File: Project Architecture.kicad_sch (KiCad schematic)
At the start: 0 parts

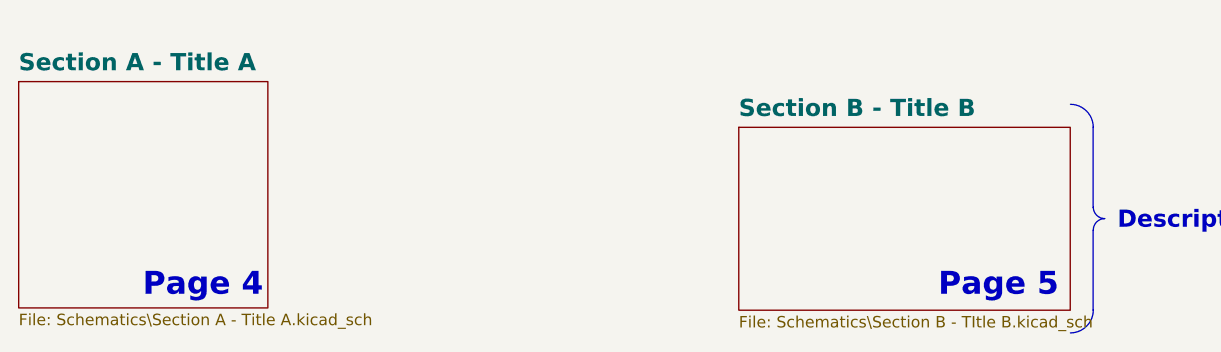
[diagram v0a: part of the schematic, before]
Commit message: Add Power Budget Sheet
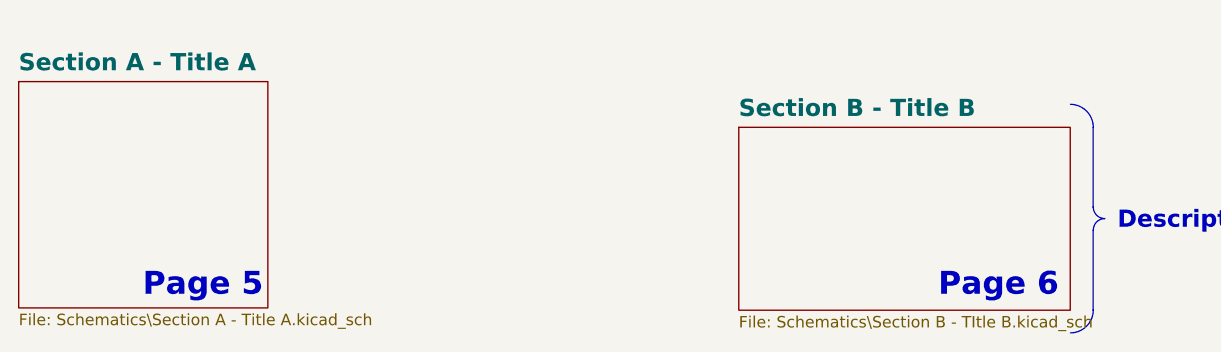
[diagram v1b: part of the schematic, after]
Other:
- note added: "Page 6"
- note removed: "Page 4"
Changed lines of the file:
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@@
 		)
 	)
-	(text "Page 4"
+	(text "Page 5"
 		(exclude_from_sim no)
 		(at 151.638 104.14 0)
@@
 			)
 			(justify right bottom)
-			(href "#4")
+			(href "#5")
 		)
 	)
-	(text "Page 5"
+	(text "Page 6"
 		(exclude_from_sim no)
 		(at 240.03 104.14 0)
@@
 			)
 			(justify right bottom)
-			(href "#5")
+			(href "#6")
 		)
 	)
@@
 			(project "SkyForge_Controller"
 				(path "/0650c7a8-acba-429c-9f8e-eec0baf0bc1c/fede4c36-00cc-4d3d-b71c-5243ba232202"
-					(page "4")
+					(page "5")
 				)
 			)
@@
 			(project "SkyForge_Controller"
 				(path "/0650c7a8-acba-429c-9f8e-eec0baf0bc1c/fede4c36-00cc-4d3d-b71c-5243ba232202"
-					(page "5")
+					(page "6")
 				)
 			)

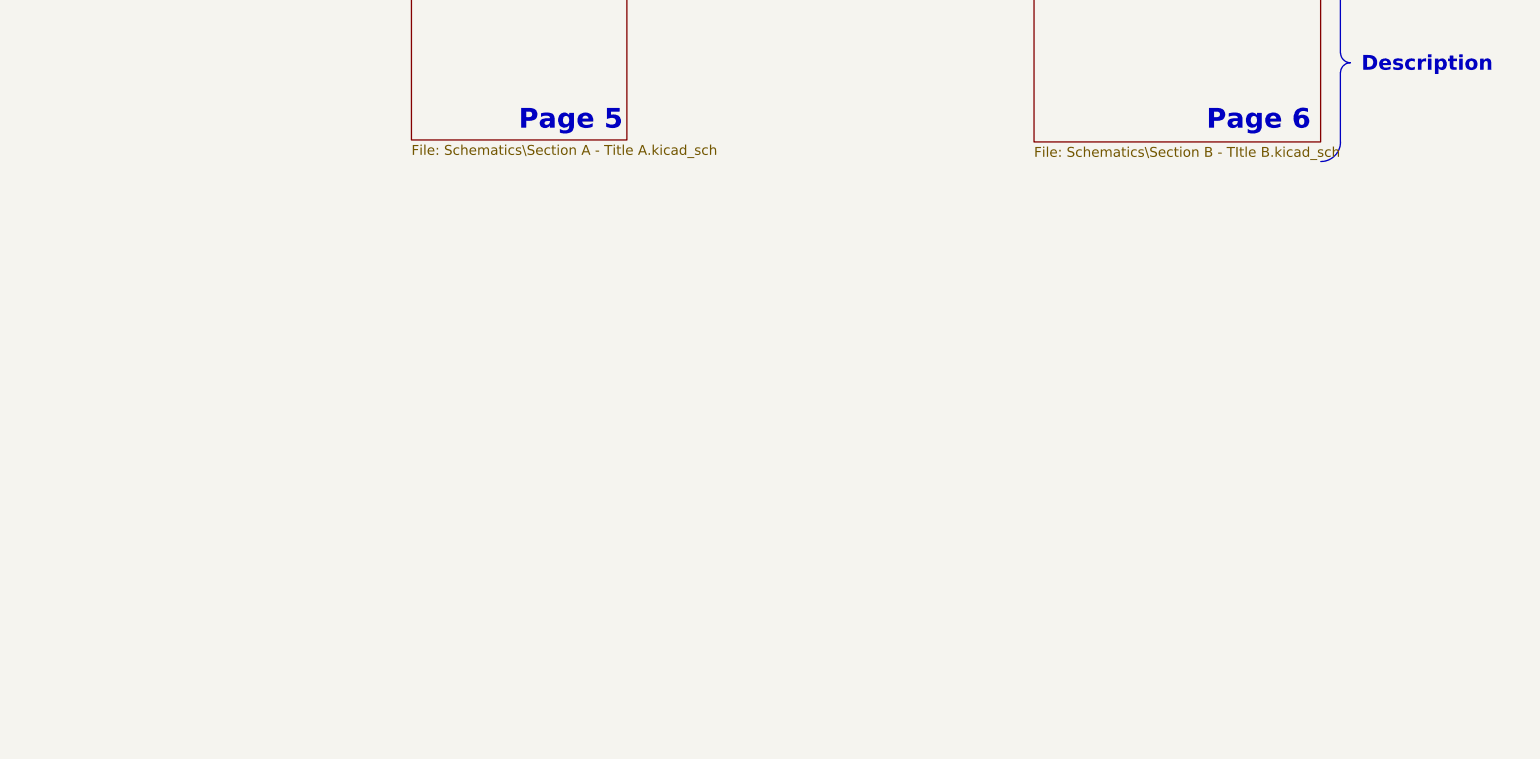
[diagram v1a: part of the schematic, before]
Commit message: Add MCU to schematic
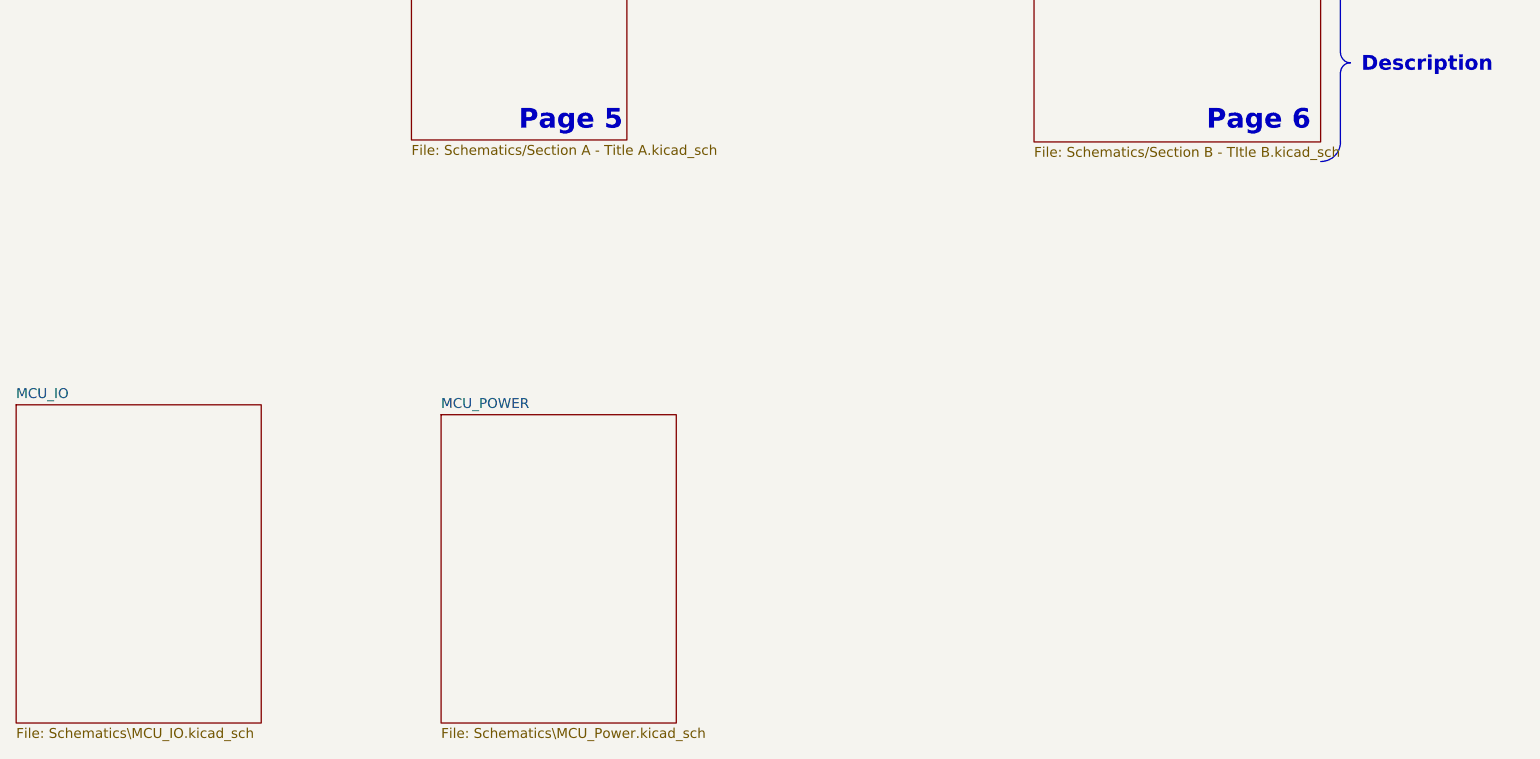
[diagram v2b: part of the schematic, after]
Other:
- added sheet MCU_IO (Schematics\MCU_IO.kicad_sch)
- added sheet MCU_POWER (Schematics\MCU_Power.kicad_sch)
- sheet Section A - Title A: file Schematics\Section A - Title A.kicad_sch -> Schematics/Section A - Title A.kicad_sch
- sheet Section B - Title B: file Schematics\Section B - TItle B.kicad_sch -> Schematics/Section B - TItle B.kicad_sch
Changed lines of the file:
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@@
+	)
+	(sheet
+		(at 73.66 139.192)
+		(size 31.496 40.894)
+		(exclude_from_sim no)
+		(in_bom yes)
+		(on_board yes)
+		(dnp no)
+		(fields_autoplaced yes)
+		(stroke
+			(width 0.1524)
+			(type solid)
+		)
+		(fill
+			(color 0 0 0 0)
+		)
+		(property "Sheetname" "MCU_IO"
+			(at 73.66 138.4804 0)
+			(show_name no)
+			(do_not_autoplace no)
+			(effects
+				(font
+					(size 1.27 1.27)
+				)
+				(justify left bottom)
+			)
+		)
+		(property "Sheetfile" "Schematics\\MCU_IO.kicad_sch"
+			(at 73.66 180.6706 0)
+			(show_name no)
+			(do_not_autoplace no)
+			(effects
+				(font
+					(size 1.27 1.27)
+				)
+				(justify left top)
+			)
+		)
+		(instances
+			(project "SkyForge_Controller"
+				(path "/0650c7a8-acba-429c-9f8e-eec0baf0bc1c/fede4c36-00cc-4d3d-b71c-5243ba232202"
+					(page "8")
+				)
+			)
+		)
 	)
 	(sheet
@@
 			)
 		)
-		(property "Sheetfile" "Schematics\\Section A - Title A.kicad_sch"
+		(property "Sheetfile" "Schematics/Section A - Title A.kicad_sch"
 			(at 124.46 105.7406 0)
 			(show_name no)
@@
 				(path "/0650c7a8-acba-429c-9f8e-eec0baf0bc1c/fede4c36-00cc-4d3d-b71c-5243ba232202"
 					(page "5")
+				)
+			)
+		)
+	)
+	(sheet
+		(at 128.27 140.462)
+		(size 30.226 39.624)
+		(exclude_from_sim no)
+		(in_bom yes)
+		(on_board yes)
+		(dnp no)
+		(fields_autoplaced yes)
+		(stroke
+			(width 0.1524)
+			(type solid)
+		)
+		(fill
+			(color 0 0 0 0)
+		)
+		(property "Sheetname" "MCU_POWER"
+			(at 128.27 139.7504 0)
+			(show_name no)
+			(do_not_autoplace no)
+			(effects
+				(font
+					(size 1.27 1.27)
+				)
+				(justify left bottom)
+			)
+		)
+		(property "Sheetfile" "Schematics\\MCU_Power.kicad_sch"
+			(at 128.27 180.6706 0)
+			(show_name no)
+			(do_not_autoplace no)
+			(effects
+				(font
+					(size 1.27 1.27)
+				)
+				(justify left top)
+			)
+		)
+		(instances
+			(project "SkyForge_Controller"
+				(path "/0650c7a8-acba-429c-9f8e-eec0baf0bc1c/fede4c36-00cc-4d3d-b71c-5243ba232202"
+					(page "9")
 				)
 			)
@@
 			)
 		)
-		(property "Sheetfile" "Schematics\\Section B - TItle B.kicad_sch"
+		(property "Sheetfile" "Schematics/Section B - TItle B.kicad_sch"
 			(at 204.47 105.9946 0)
 			(show_name no)

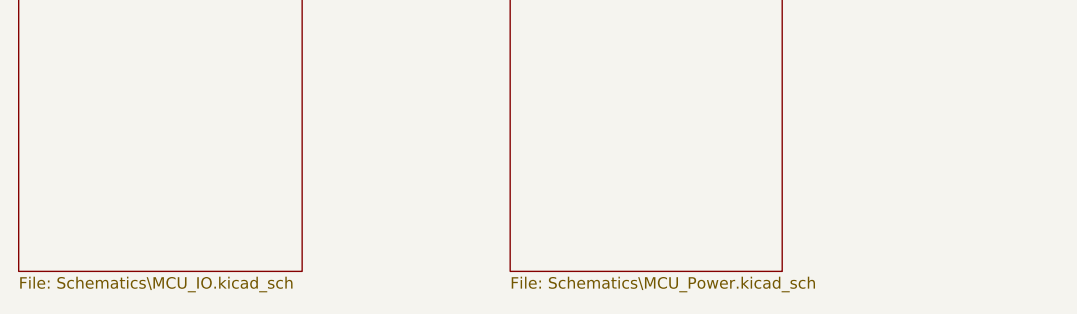
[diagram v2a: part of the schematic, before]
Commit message: Add MCU Power schematic
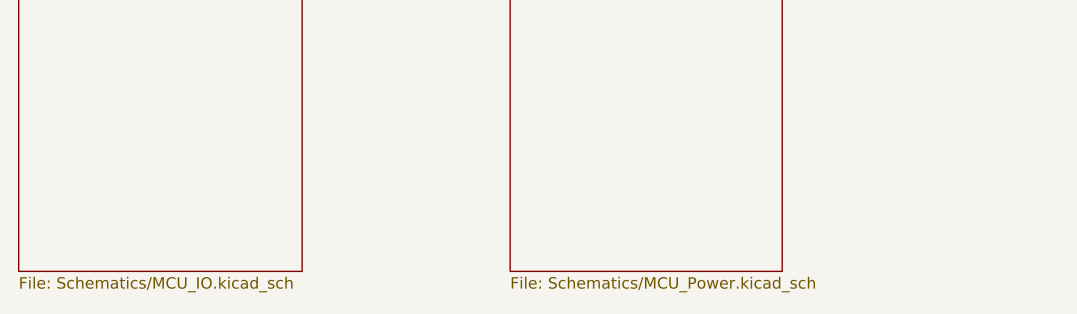
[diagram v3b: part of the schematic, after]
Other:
- sheet MCU_IO: file Schematics\MCU_IO.kicad_sch -> Schematics/MCU_IO.kicad_sch
- sheet MCU_POWER: file Schematics\MCU_Power.kicad_sch -> Schematics/MCU_Power.kicad_sch
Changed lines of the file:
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@@
 			)
 		)
-		(property "Sheetfile" "Schematics\\MCU_IO.kicad_sch"
+		(property "Sheetfile" "Schematics/MCU_IO.kicad_sch"
 			(at 73.66 180.6706 0)
 			(show_name no)
@@
 			)
 		)
-		(property "Sheetfile" "Schematics\\MCU_Power.kicad_sch"
+		(property "Sheetfile" "Schematics/MCU_Power.kicad_sch"
 			(at 128.27 180.6706 0)
 			(show_name no)

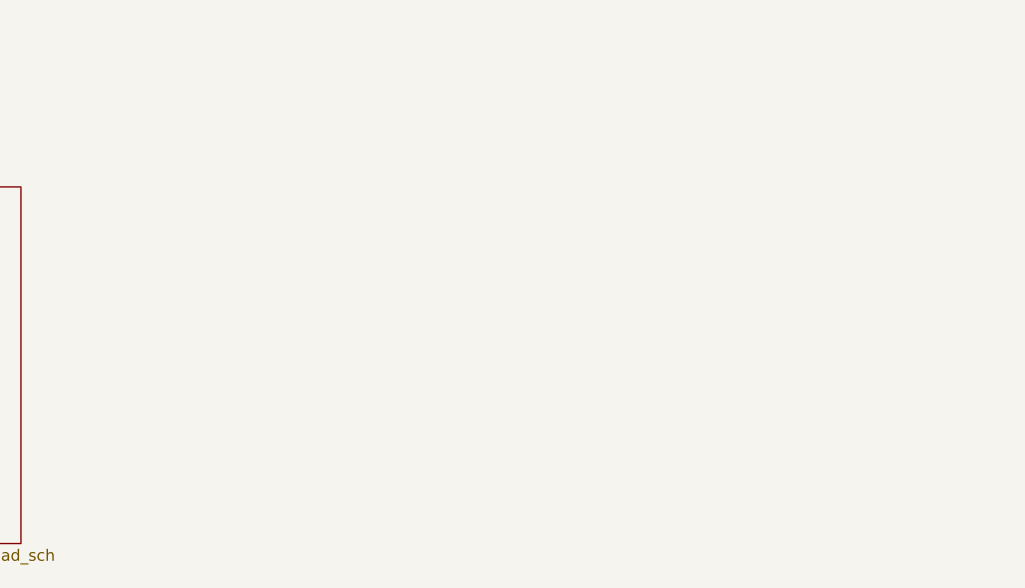
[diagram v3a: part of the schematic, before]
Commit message: Add Power Conversion & Selection Ckt and SWD Debug connector
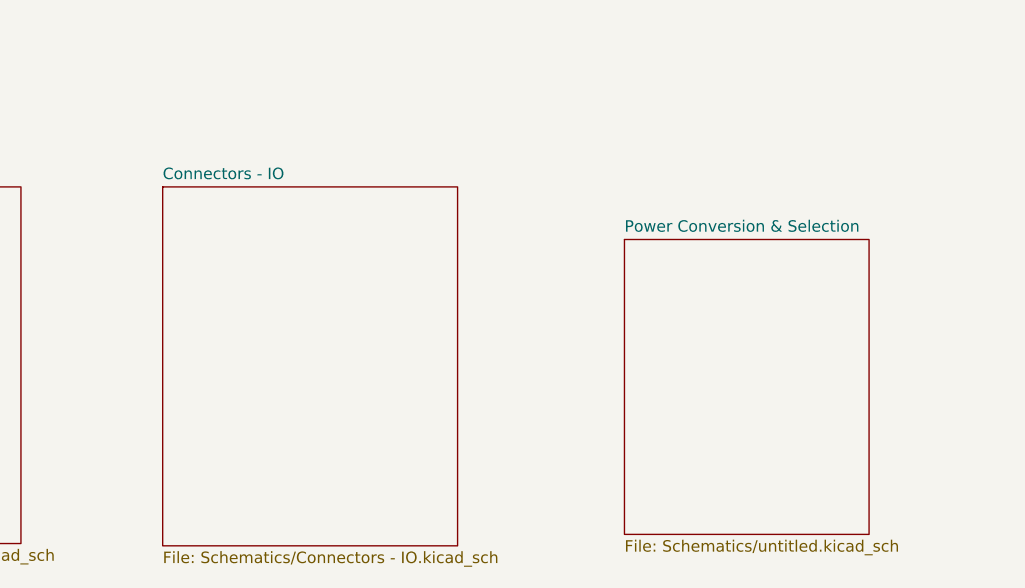
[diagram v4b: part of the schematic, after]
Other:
- added sheet Connectors - IO (Schematics/Connectors - IO.kicad_sch)
- added sheet Power Conversion & Selection (Schematics/untitled.kicad_sch)
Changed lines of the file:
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@@
+	)
+	(sheet
+		(at 225.552 146.304)
+		(size 27.178 32.766)
+		(exclude_from_sim no)
+		(in_bom yes)
+		(on_board yes)
+		(dnp no)
+		(fields_autoplaced yes)
+		(stroke
+			(width 0.1524)
+			(type solid)
+		)
+		(fill
+			(color 0 0 0 0)
+		)
+		(property "Sheetname" "Power Conversion & Selection"
+			(at 225.552 145.5924 0)
+			(show_name no)
+			(do_not_autoplace no)
+			(effects
+				(font
+					(size 1.27 1.27)
+				)
+				(justify left bottom)
+			)
+		)
+		(property "Sheetfile" "Schematics/untitled.kicad_sch"
+			(at 225.552 179.6546 0)
+			(show_name no)
+			(do_not_autoplace no)
+			(effects
+				(font
+					(size 1.27 1.27)
+				)
+				(justify left top)
+			)
+		)
+		(instances
+			(project "SkyForge_Controller"
+				(path "/0650c7a8-acba-429c-9f8e-eec0baf0bc1c/fede4c36-00cc-4d3d-b71c-5243ba232202"
+					(page "12")
+				)
+			)
+		)
 	)
 	(sheet
@@
 				)
 			)
+		)
+	)
+	(sheet
+		(at 174.244 140.462)
+		(size 32.766 39.878)
+		(exclude_from_sim no)
+		(in_bom yes)
+		(on_board yes)
+		(dnp no)
+		(fields_autoplaced yes)
+		(stroke
+			(width 0.1524)
+			(type solid)
+		)
+		(fill
+			(color 0 0 0 0)
+		)
+		(property "Sheetname" "Connectors - IO"
+			(at 174.244 139.7504 0)
+			(show_name no)
+			(do_not_autoplace no)
+			(effects
+				(font
+					(size 1.27 1.27)
+				)
+				(justify left bottom)
+			)
+		)
+		(property "Sheetfile" "Schematics/Connectors - IO.kicad_sch"
+			(at 174.244 180.9246 0)
+			(show_name no)
+			(do_not_autoplace no)
+			(effects
+				(font
+					(size 1.27 1.27)
+				)
+				(justify left top)
+			)
+		)
+		(instances
+			(project "SkyForge_Controller"
+				(path "/0650c7a8-acba-429c-9f8e-eec0baf0bc1c/fede4c36-00cc-4d3d-b71c-5243ba232202"
+					(page "11")
+				)
+			)

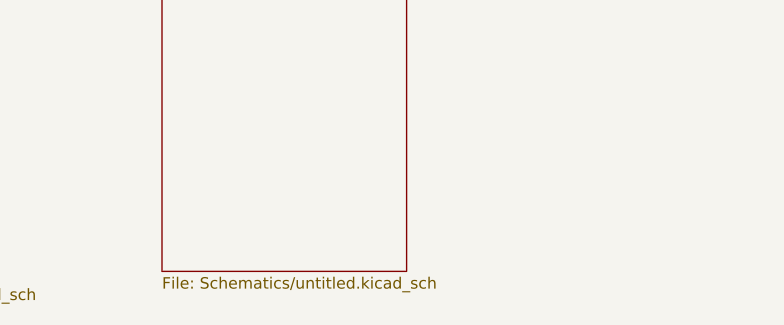
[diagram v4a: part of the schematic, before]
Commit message: Add external Power connector and Power conversion & Selection ckt
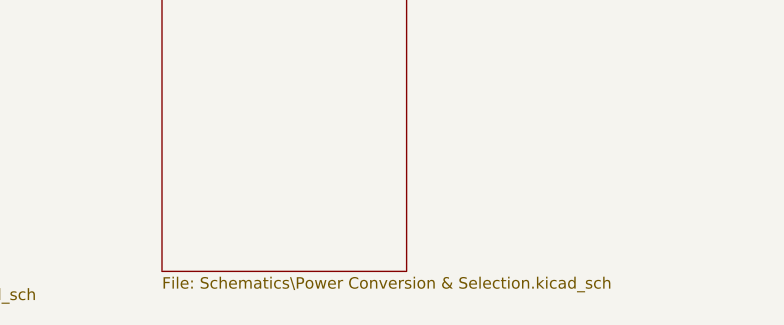
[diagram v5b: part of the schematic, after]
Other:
- sheet Power Conversion & Selection: file Schematics/untitled.kicad_sch -> Schematics\Power Conversion & Selection.kicad_sch
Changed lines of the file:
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@@
 			)
 		)
-		(property "Sheetfile" "Schematics/untitled.kicad_sch"
+		(property "Sheetfile" "Schematics\\Power Conversion & Selection.kicad_sch"
 			(at 225.552 179.6546 0)
 			(show_name no)

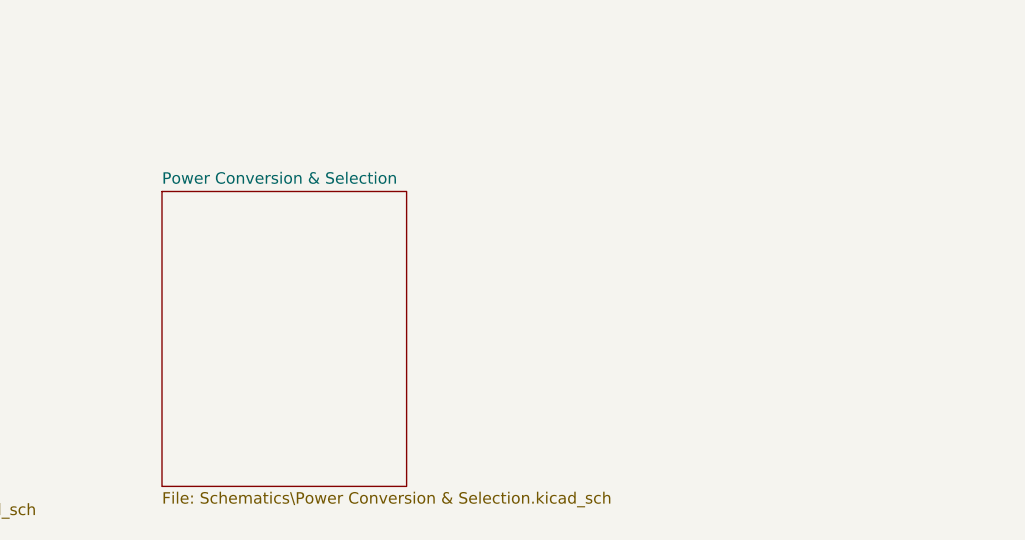
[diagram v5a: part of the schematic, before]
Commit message: Add USB
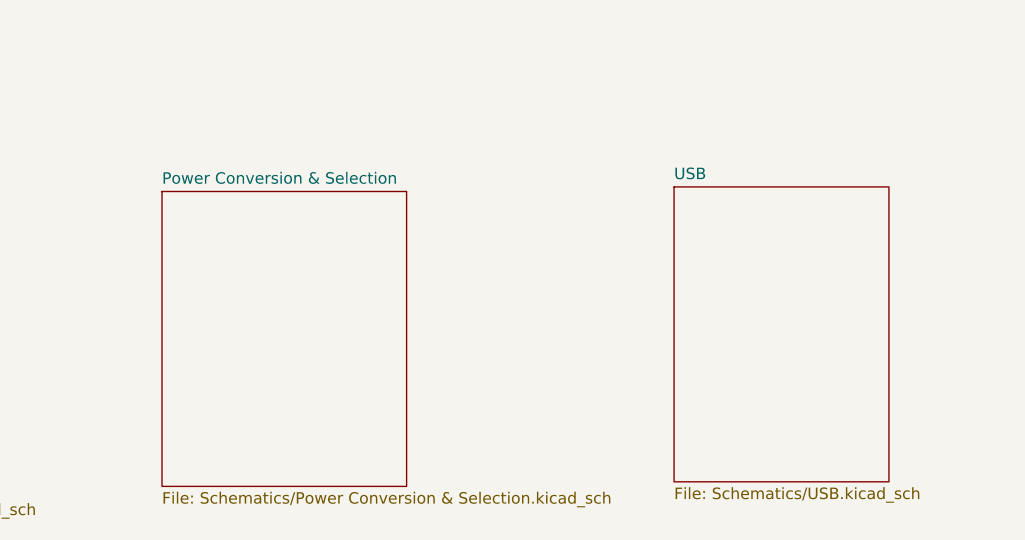
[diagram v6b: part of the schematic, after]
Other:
- added sheet USB (Schematics/USB.kicad_sch)
- sheet Power Conversion & Selection: file Schematics\Power Conversion & Selection.kicad_sch -> Schematics/Power Conversion & Selection.kicad_sch
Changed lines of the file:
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@@
 			)
 		)
-		(property "Sheetfile" "Schematics\\Power Conversion & Selection.kicad_sch"
+		(property "Sheetfile" "Schematics/Power Conversion & Selection.kicad_sch"
 			(at 225.552 179.6546 0)
 			(show_name no)
@@
 				)
 			)
+		)
+	)
+	(sheet
+		(at 282.448 145.796)
+		(size 23.876 32.766)
+		(exclude_from_sim no)
+		(in_bom yes)
+		(on_board yes)
+		(dnp no)
+		(fields_autoplaced yes)
+		(stroke
+			(width 0.1524)
+			(type solid)
+		)
+		(fill
+			(color 0 0 0 0)
+		)
+		(property "Sheetname" "USB"
+			(at 282.448 145.0844 0)
+			(show_name no)
+			(do_not_autoplace no)
+			(effects
+				(font
+					(size 1.27 1.27)
+				)
+				(justify left bottom)
+			)
+		)
+		(property "Sheetfile" "Schematics/USB.kicad_sch"
+			(at 282.448 179.1466 0)
+			(show_name no)
+			(do_not_autoplace no)
+			(effects
+				(font
+					(size 1.27 1.27)
+				)
+				(justify left top)
+			)
+		)
+		(instances
+			(project "SkyForge_Controller"
+				(path "/0650c7a8-acba-429c-9f8e-eec0baf0bc1c/fede4c36-00cc-4d3d-b71c-5243ba232202"
+					(page "13")
+				)
+			)
